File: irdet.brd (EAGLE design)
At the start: 50 x 45 mm, 66 parts, among them IC1 MEGA8-AI, IC2 78L05F, J1 PSH02-04WG, J2 PSH02-04WG, J3 PSH02-04WG, J4 PSH02-04WG, J5 22-05-7098-09, T1 S9013, T2 S9012, T3 S9013, T4 S9012, T5 S9013, T6 S9012, T7 S9013, T8 S9012, X1 ARK500/2, X2 ARK500/2

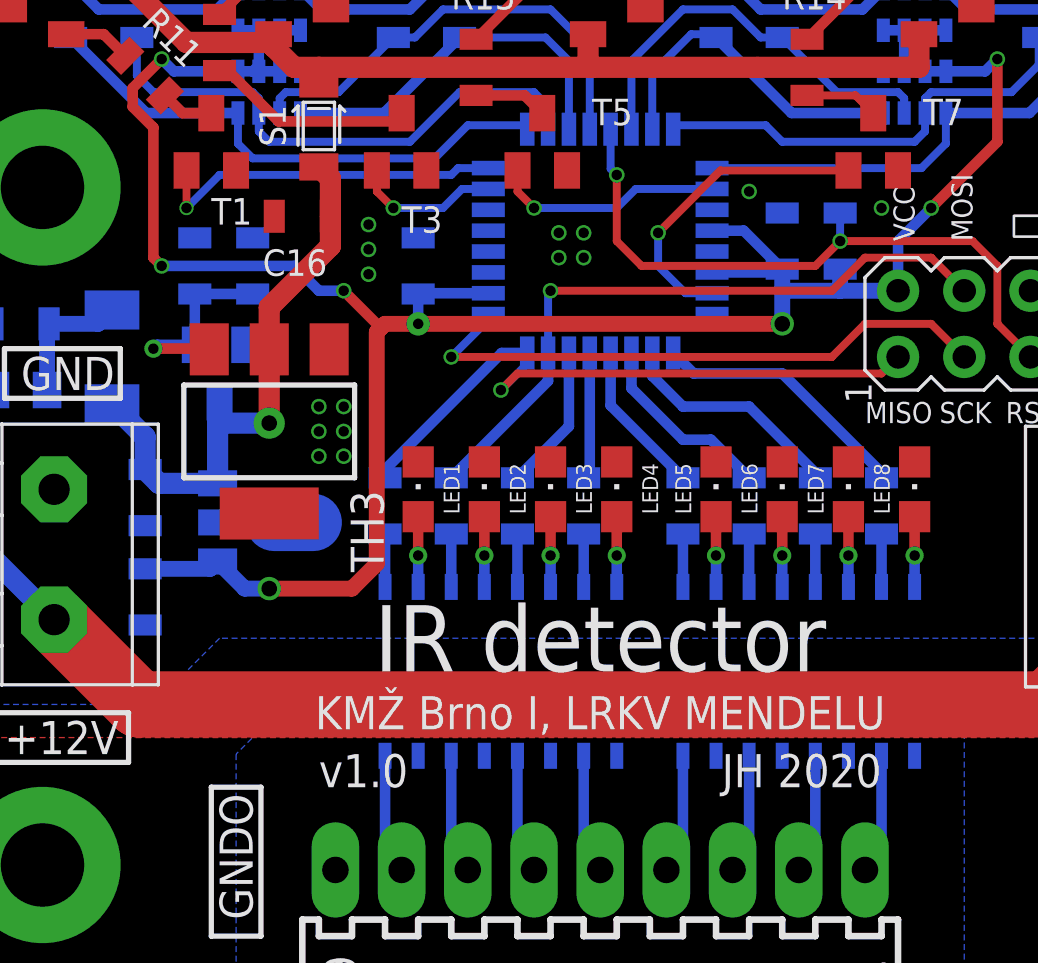
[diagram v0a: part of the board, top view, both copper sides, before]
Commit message: Move 22u capacitors to bottom layer.
So all the capacitors could be soldered automatically.
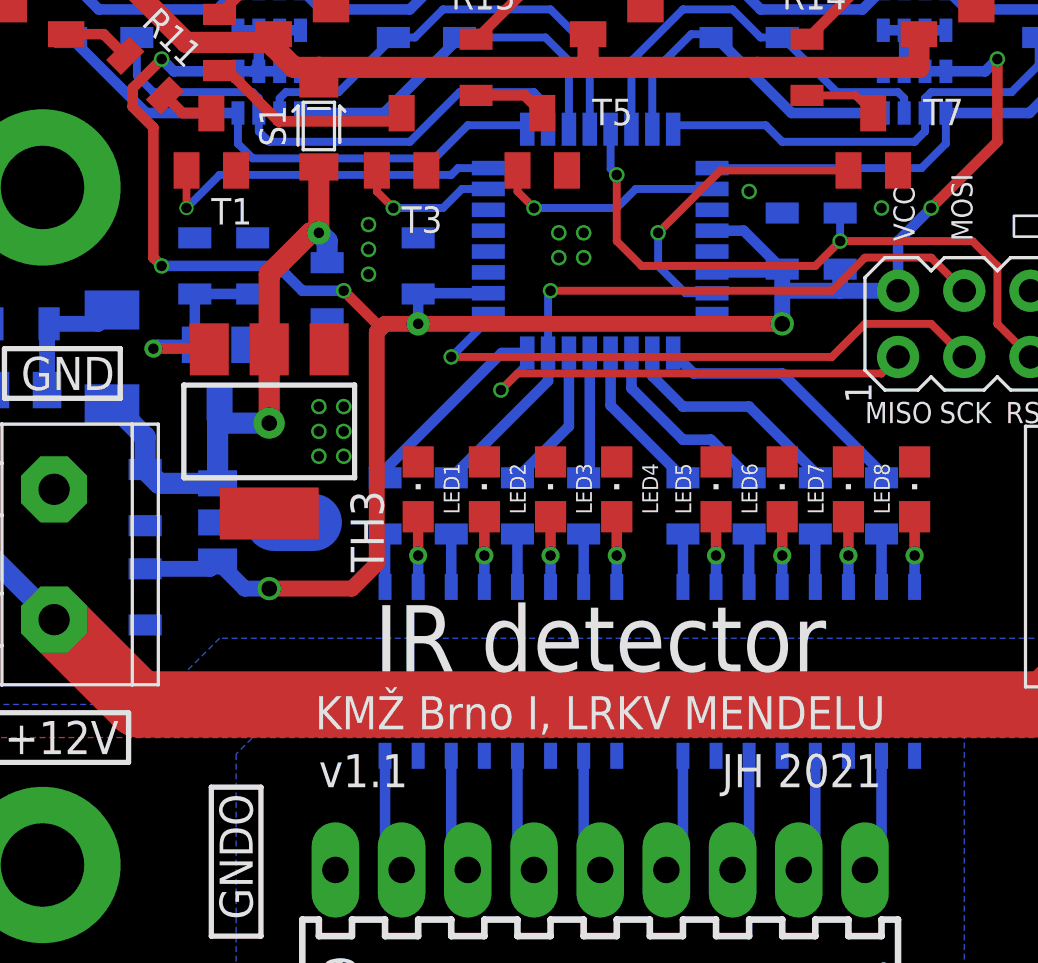
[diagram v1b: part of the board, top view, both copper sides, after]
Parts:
- moved C16 3.01 mm to (14.9, 26.0), flipped to the bottom, turned to 270 degrees
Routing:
- net +12V: track 22.2 -> 23.3 mm, vias 1 -> 2
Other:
- board text added: "JH 2021"
- board text added: "v1.1"
- board text removed: "JH 2020"
- board text removed: "v1.0"
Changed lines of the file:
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@@
 <text x="25.4" y="11.43" size="2.54" layer="25" align="bottom-center">IR detector</text>
 <text x="25.4" y="9.2075" size="1.27" layer="25" align="bottom-center">KMŽ Brno I, LRKV MENDELU</text>
-<text x="36.195" y="6.985" size="1.27" layer="25" align="bottom-right">JH 2020</text>
-<text x="14.605" y="6.985" size="1.27" layer="25">v1.0</text>
+<text x="36.195" y="6.985" size="1.27" layer="25" align="bottom-right">JH 2021</text>
+<text x="14.605" y="6.985" size="1.27" layer="25">v1.1</text>
 <text x="42.545" y="27.94" size="1.27" layer="25" rot="R90">⏚</text>
 <text x="37.465" y="27.94" size="0.8128" layer="25" rot="R90">VCC</text>
@@
 <attribute name="VALUE" x="46.0375" y="35.56" size="1.016" layer="28" rot="MR90"/>
 </element>
-<element name="C16" library="rcl" package="C0805" value="22u" x="13.97" y="28.8925" smashed="yes" rot="R180">
-<attribute name="NAME" x="14.9225" y="27.6225" size="1.016" layer="25" rot="R180"/>
-<attribute name="VALUE" x="15.24" y="27.94" size="1.016" layer="27" rot="R180"/>
+<element name="C16" library="rcl" package="C0805" value="22u" x="14.9225" y="26.035" smashed="yes" rot="MR270">
+<attribute name="NAME" x="14.605" y="24.13" size="1.016" layer="26" rot="MR180"/>
+<attribute name="VALUE" x="13.97" y="27.305" size="1.016" layer="28" rot="MR270"/>
 </element>
 <element name="C2" library="rcl" package="C0805" value="100n" x="32.385" y="27.94" smashed="yes" rot="MR270">
@@
 </element>
 <element name="R2" library="rcl" package="R0805" value="2k2" x="12.065" y="26.9875" smashed="yes" rot="MR270">
-<attribute name="NAME" x="14.2875" y="27.94" size="1.016" layer="26" rot="MR270"/>
+<attribute name="NAME" x="11.43" y="29.845" size="1.016" layer="26" rot="MR180"/>
 <attribute name="VALUE" x="11.7475" y="29.845" size="1.016" layer="28" rot="MR180"/>
 </element>
@@
 <wire x1="8.255" y1="27.305" x2="8.5725" y2="26.9875" width="0.4064" layer="1"/>
 <via x="8.5725" y="26.9875" extent="1-16" drill="0.4" diameter="0.6"/>
-<wire x1="13.6525" y1="26.9875" x2="14.605" y2="26.035" width="0.4064" layer="16"/>
-<wire x1="14.605" y1="26.035" x2="15.5575" y2="26.035" width="0.4064" layer="16"/>
+<wire x1="13.0175" y1="26.9875" x2="13.97" y2="26.035" width="0.4064" layer="16"/>
+<wire x1="13.97" y1="26.035" x2="15.5575" y2="26.035" width="0.4064" layer="16"/>
 <via x="15.5575" y="26.035" extent="1-16" drill="0.4" diameter="0.6"/>
-<wire x1="8.5725" y1="26.9875" x2="13.6525" y2="26.9875" width="0.4064" layer="16"/>
+<wire x1="8.5725" y1="26.9875" x2="13.0175" y2="26.9875" width="0.4064" layer="16"/>
 <wire x1="15.5575" y1="26.035" x2="16.98625" y2="24.60625" width="0.4064" layer="1"/>
 </signal>
@@
 <wire x1="12.7" y1="23.7875" x2="12.7" y2="20.955" width="0.8128" layer="1"/>
 <via x="12.7" y="20.955" extent="1-16" drill="0.6" diameter="1.2"/>
-<wire x1="14.605" y1="30.785" x2="15.047" y2="30.343" width="0.8128" layer="1"/>
-<wire x1="15.047" y1="30.343" x2="15.047" y2="28.8925" width="0.8128" layer="1"/>
-<wire x1="12.7" y1="23.7875" x2="12.7" y2="25.4" width="0.8128" layer="1"/>
-<wire x1="15.047" y1="27.747" x2="15.047" y2="28.8925" width="0.8128" layer="1"/>
-<wire x1="12.7" y1="25.4" x2="15.047" y2="27.747" width="0.8128" layer="1"/>
+<wire x1="12.7" y1="23.7875" x2="12.7" y2="26.67" width="0.8128" layer="1"/>
 <wire x1="12.7" y1="20.955" x2="10.719" y2="20.955" width="0.8128" layer="16"/>
+<wire x1="14.605" y1="30.785" x2="14.605" y2="28.2575" width="0.8128" layer="1"/>
+<wire x1="14.605" y1="28.2575" x2="14.2875" y2="28.2575" width="0.8128" layer="1"/>
+<wire x1="14.2875" y1="28.2575" x2="12.7" y2="26.67" width="0.8128" layer="1"/>
+<wire x1="14.9225" y1="27.112" x2="14.9225" y2="27.94" width="0.8128" layer="16"/>
+<wire x1="14.9225" y1="27.94" x2="14.605" y2="28.2575" width="0.8128" layer="16"/>
+<via x="14.605" y="28.2575" extent="1-16" drill="0.4" diameter="0.9"/>
 </signal>
 <signal name="N$13">

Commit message: TLP290 → TLP292.
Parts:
- OK1, OK2: value TLP290 -> TLP292
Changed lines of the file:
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@@
 <attribute name="VALUE" x="28.575" y="17.145" size="1.27" layer="27" rot="R90"/>
 </element>
-<element name="OK2" library="optocoupler" library_urn="urn:adsk.eagle:library:320" package="MINI-FLAT-16" package3d_urn="urn:adsk.eagle:package:21967/1" value="TLP290" x="33.02" y="11.43" smashed="yes" rot="MR270">
+<element name="OK2" library="optocoupler" library_urn="urn:adsk.eagle:library:320" package="MINI-FLAT-16" package3d_urn="urn:adsk.eagle:package:21967/1" value="TLP292" x="33.02" y="11.43" smashed="yes" rot="MR270">
 <attribute name="MF" value="" x="58.42" y="-31.75" size="1.778" layer="28" rot="MR270" display="off"/>
 <attribute name="MPN" value="" x="58.42" y="-31.75" size="1.778" layer="28" rot="MR270" display="off"/>
@@
 <attribute name="VALUE" x="31.115" y="12.065" size="1.016" layer="28" rot="MR180"/>
 </element>
-<element name="OK1" library="optocoupler" library_urn="urn:adsk.eagle:library:320" package="MINI-FLAT-16" package3d_urn="urn:adsk.eagle:package:21967/1" value="TLP290" x="21.59" y="11.43" smashed="yes" rot="MR270">
+<element name="OK1" library="optocoupler" library_urn="urn:adsk.eagle:library:320" package="MINI-FLAT-16" package3d_urn="urn:adsk.eagle:package:21967/1" value="TLP292" x="21.59" y="11.43" smashed="yes" rot="MR270">
 <attribute name="MF" value="" x="46.99" y="-40.64" size="1.778" layer="28" rot="MR270" display="off"/>
 <attribute name="MPN" value="" x="46.99" y="-40.64" size="1.778" layer="28" rot="MR270" display="off"/>

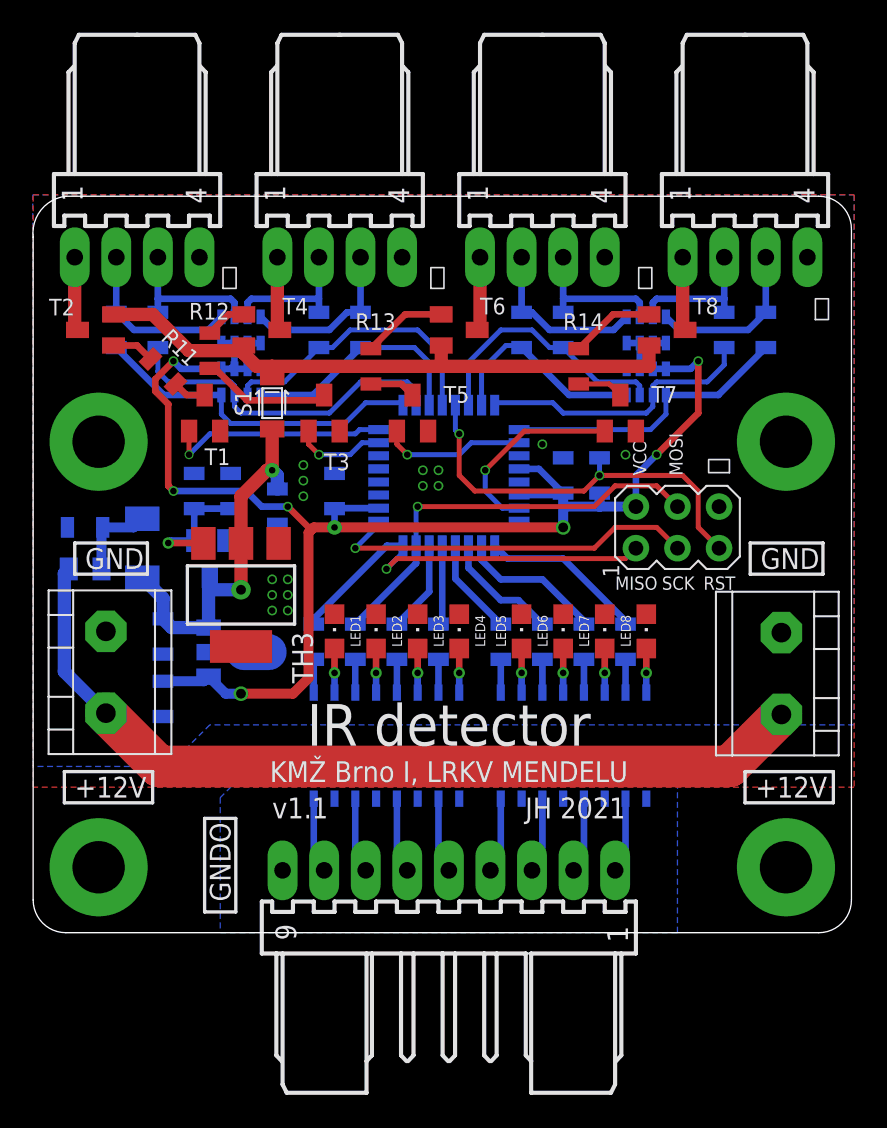
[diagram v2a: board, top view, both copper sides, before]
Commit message: Use proper connectors (MVE252-5-V).
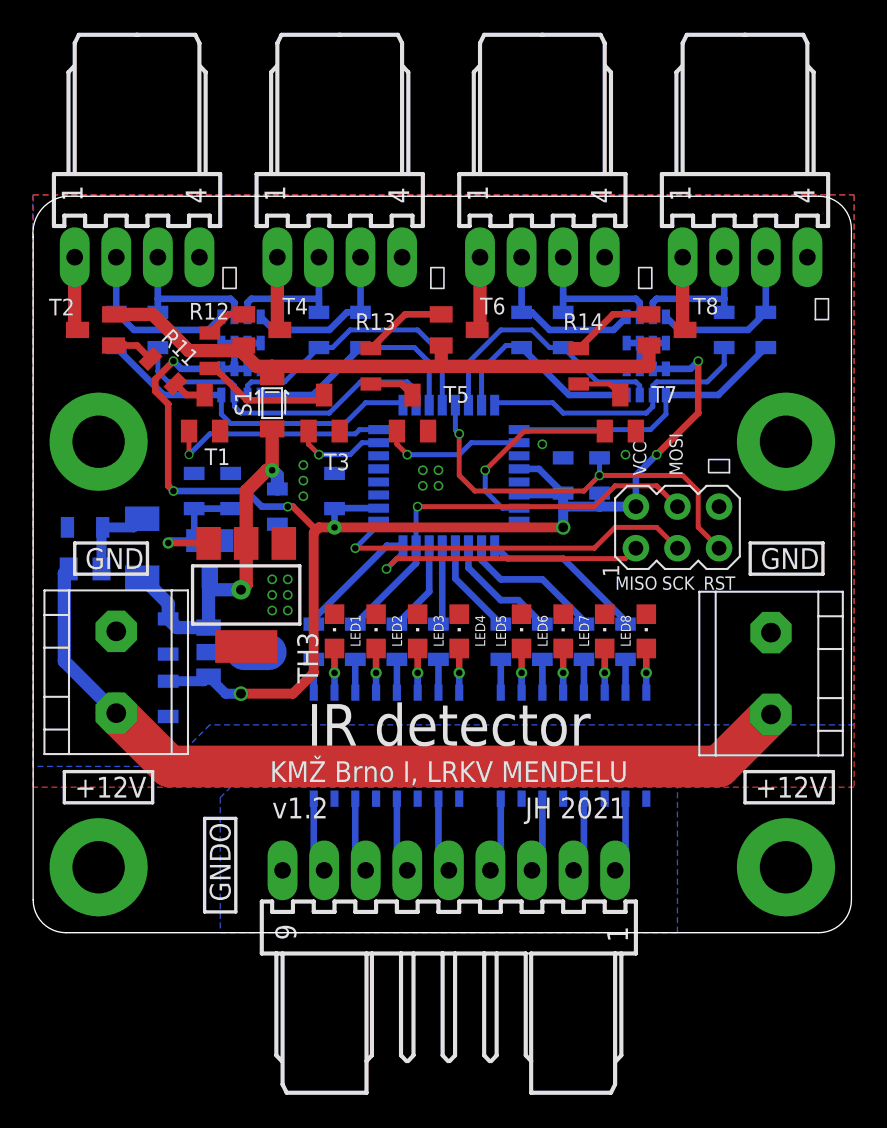
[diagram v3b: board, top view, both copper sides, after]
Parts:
- X1, X2: value ARK500/2 -> MVE252-5-V; device con-malina:ARK500/2 -> con-malina:MVE252-5-V
- moved X1 0.63 mm to (5.08, 18.4)
- moved X2 0.63 mm to (45.1, 13.3)
- moved C7 0.32 mm to (8.26, 18.1)
- moved C8 0.32 mm to (8.26, 14.3)
- moved TH3 0.32 mm to (13.0, 20.6)
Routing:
- net +12VIN: track 53.9 -> 52.9 mm
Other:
- board text added: "v1.2"
- board text removed: "v1.1"

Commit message: Change transistors to more common.
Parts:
- T1, T3, T5, T7: value S9013 -> BC847
- T2, T6, T8: value S9012 -> BC857
- T4: value S9012 -> BC587
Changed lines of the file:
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@@
 <attribute name="NAME" x="13.335" y="31.5675" size="1.016" layer="25" rot="R90"/>
 </element>
-<element name="T1" library="transistor" library_urn="urn:adsk.eagle:library:402" package="SOT23-BEC" package3d_urn="urn:adsk.eagle:package:28748/2" value="S9013" x="10.4775" y="31.75" smashed="yes">
+<element name="T1" library="transistor" library_urn="urn:adsk.eagle:library:402" package="SOT23-BEC" package3d_urn="urn:adsk.eagle:package:28748/2" value="BC847" x="10.4775" y="31.75" smashed="yes">
 <attribute name="NAME" x="10.4775" y="28.575" size="1.016" layer="25"/>
 <attribute name="POPULARITY" value="0" x="63.8175" y="-7.62" size="1.778" layer="27" display="off"/>
 <attribute name="VALUE" x="8.255" y="28.8925" size="1.016" layer="27"/>
 </element>
-<element name="T2" library="transistor" library_urn="urn:adsk.eagle:library:402" package="SOT23-BEC" package3d_urn="urn:adsk.eagle:package:28748/2" value="S9012" x="3.81" y="36.83" smashed="yes" rot="R90">
+<element name="T2" library="transistor" library_urn="urn:adsk.eagle:library:402" package="SOT23-BEC" package3d_urn="urn:adsk.eagle:package:28748/2" value="BC857" x="3.81" y="36.83" smashed="yes" rot="R90">
 <attribute name="NAME" x="2.54" y="38.735" size="1.016" layer="25" rot="R180"/>
 <attribute name="POPULARITY" value="0" x="43.18" y="96.52" size="1.778" layer="27" rot="R90" display="off"/>
 <attribute name="VALUE" x="1.905" y="34.29" size="1.016" layer="27" rot="R90"/>
 </element>
-<element name="T3" library="transistor" library_urn="urn:adsk.eagle:library:402" package="SOT23-BEC" package3d_urn="urn:adsk.eagle:package:28748/2" value="S9013" x="17.78" y="31.75" smashed="yes">
+<element name="T3" library="transistor" library_urn="urn:adsk.eagle:library:402" package="SOT23-BEC" package3d_urn="urn:adsk.eagle:package:28748/2" value="BC847" x="17.78" y="31.75" smashed="yes">
 <attribute name="NAME" x="17.78" y="28.2575" size="1.016" layer="25"/>
 <attribute name="POPULARITY" value="0" x="83.82" y="-7.62" size="1.778" layer="27" display="off"/>
 <attribute name="VALUE" x="18.0975" y="29.845" size="1.016" layer="27" rot="R270"/>
 </element>
-<element name="T4" library="transistor" library_urn="urn:adsk.eagle:library:402" package="SOT23-BEC" package3d_urn="urn:adsk.eagle:package:28748/2" value="S9012" x="13.97" y="36.83" smashed="yes" rot="R270">
+<element name="T4" library="transistor" library_urn="urn:adsk.eagle:library:402" package="SOT23-BEC" package3d_urn="urn:adsk.eagle:package:28748/2" value="BC587" x="13.97" y="36.83" smashed="yes" rot="R270">
 <attribute name="NAME" x="15.24" y="37.7825" size="1.016" layer="25"/>
 <attribute name="POPULARITY" value="0" x="-25.4" y="-35.56" size="1.778" layer="27" rot="R270" display="off"/>
 <attribute name="VALUE" x="15.875" y="38.735" size="1.016" layer="27" rot="R270"/>
 </element>
-<element name="T5" library="transistor" library_urn="urn:adsk.eagle:library:402" package="SOT23-BEC" package3d_urn="urn:adsk.eagle:package:28748/2" value="S9013" x="23.1775" y="31.75" smashed="yes">
+<element name="T5" library="transistor" library_urn="urn:adsk.eagle:library:402" package="SOT23-BEC" package3d_urn="urn:adsk.eagle:package:28748/2" value="BC847" x="23.1775" y="31.75" smashed="yes">
 <attribute name="NAME" x="25.0825" y="32.385" size="1.016" layer="25"/>
 <attribute name="POPULARITY" value="0" x="39.6875" y="-17.78" size="1.778" layer="27" display="off"/>
 <attribute name="VALUE" x="25.0825" y="31.75" size="1.016" layer="27"/>
 </element>
-<element name="T6" library="transistor" library_urn="urn:adsk.eagle:library:402" package="SOT23-BEC" package3d_urn="urn:adsk.eagle:package:28748/2" value="S9012" x="26.035" y="36.83" smashed="yes" rot="R270">
+<element name="T6" library="transistor" library_urn="urn:adsk.eagle:library:402" package="SOT23-BEC" package3d_urn="urn:adsk.eagle:package:28748/2" value="BC857" x="26.035" y="36.83" smashed="yes" rot="R270">
 <attribute name="NAME" x="27.305" y="37.7825" size="1.016" layer="25"/>
 <attribute name="POPULARITY" value="0" x="-23.495" y="13.97" size="1.778" layer="27" rot="R270" display="off"/>
 <attribute name="VALUE" x="22.86" y="38.735" size="1.016" layer="27" rot="R270"/>
 </element>
-<element name="T7" library="transistor" library_urn="urn:adsk.eagle:library:402" package="SOT23-BEC" package3d_urn="urn:adsk.eagle:package:28748/2" value="S9013" x="35.8775" y="31.75" smashed="yes">
+<element name="T7" library="transistor" library_urn="urn:adsk.eagle:library:402" package="SOT23-BEC" package3d_urn="urn:adsk.eagle:package:28748/2" value="BC847" x="35.8775" y="31.75" smashed="yes">
 <attribute name="NAME" x="37.7825" y="32.385" size="1.016" layer="25"/>
 <attribute name="POPULARITY" value="0" x="65.0875" y="-17.78" size="1.778" layer="27" display="off"/>
 <attribute name="VALUE" x="37.7825" y="31.75" size="1.016" layer="27"/>
 </element>
-<element name="T8" library="transistor" library_urn="urn:adsk.eagle:library:402" package="SOT23-BEC" package3d_urn="urn:adsk.eagle:package:28748/2" value="S9012" x="38.735" y="36.83" smashed="yes" rot="R270">
+<element name="T8" library="transistor" library_urn="urn:adsk.eagle:library:402" package="SOT23-BEC" package3d_urn="urn:adsk.eagle:package:28748/2" value="BC857" x="38.735" y="36.83" smashed="yes" rot="R270">
 <attribute name="NAME" x="40.3225" y="37.7825" size="1.016" layer="25"/>
 <attribute name="POPULARITY" value="0" x="-10.795" y="1.27" size="1.778" layer="27" rot="R270" display="off"/>

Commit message: Fix bad part value.
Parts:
- T4: value BC587 -> BC857
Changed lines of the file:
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@@
 <attribute name="VALUE" x="18.0975" y="29.845" size="1.016" layer="27" rot="R270"/>
 </element>
-<element name="T4" library="transistor" library_urn="urn:adsk.eagle:library:402" package="SOT23-BEC" package3d_urn="urn:adsk.eagle:package:28748/2" value="BC587" x="13.97" y="36.83" smashed="yes" rot="R270">
+<element name="T4" library="transistor" library_urn="urn:adsk.eagle:library:402" package="SOT23-BEC" package3d_urn="urn:adsk.eagle:package:28748/2" value="BC857" x="13.97" y="36.83" smashed="yes" rot="R270">
 <attribute name="NAME" x="15.24" y="37.7825" size="1.016" layer="25"/>
 <attribute name="POPULARITY" value="0" x="-25.4" y="-35.56" size="1.778" layer="27" rot="R270" display="off"/>
